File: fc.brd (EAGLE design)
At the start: 160 x 100 mm, 48 parts, among them IC1 FT230XQ, IC2 BN055, U2 ATMEGA2560-16AU100A-M, Y1 16MHz, Y2 32.768kHz

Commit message: First draft of the schematic finished
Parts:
- removed R20, R21: 5.6, rcl:R0603
- added LED0, LED5, LED6, LED7: (no value), led:CHIP-LED0603
- added PPM0, PPM1, PPM2, PPM3, PPM4, PPM5, PPM6, PPM7, SBUS: (no value), pinhead:1X03
- added R10, R11, R12: 100, rcl:R0603
- added R2: (no value), resistor:R0603
- added U$1: BSS138, hwp_SS18:SOT23
- R15, R16, R17: value 10k -> 100
- R18, R19: value 5.6 -> 100
- moved C18 154.7 mm to (17.8, 26.7), turned to 180 degrees
- moved C5 154.7 mm to (17.8, 30.5), turned to 180 degrees
- moved C4 153.9 mm to (3.81, 36.8), turned to 180 degrees
- moved C3 146.3 mm to (3.81, 33.0), turned to 180 degrees
- moved Y2 145.5 mm to (14.0, 27.9), turned to 270 degrees
- moved C2 138.7 mm to (3.81, 29.2), turned to 180 degrees
- moved R1 133.0 mm to (8.89, 33.0), turned to 180 degrees
- moved C1 129.8 mm to (3.81, 25.4), turned to 180 degrees
- moved C15 123.8 mm to (61.0, 35.6)
- moved LED_RX 123.8 mm to (77.5, 44.5)
- moved LED_TX 123.8 mm to (55.9, 31.8)
- moved R4 123.8 mm to (66.0, 22.9)
- moved C16 123.8 mm to (69.8, 35.6)
- moved C17 123.8 mm to (57.1, 27.9)
- moved IC2 120.2 mm to (8.89, 27.9), turned to 270 degrees
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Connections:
- removed net !ALERT_+3V3: R17.1, U2.8
- removed net !ALERT_+5V: R16.1, U2.7
- removed net !ALERT_VBAT: R15.1, U2.6
- removed net N$14: R21.2, U2.38
- removed net N$17: R20.2, U2.37
- removed net N$19: R18.2, U2.35
- removed net N$21: LED2.A, R19.1
- removed net N$23: LED4.A, R21.1
- new net !SBUS: R2.1, U$1.3, U2.12
- new net LED0: R15.2, U2.35
- new net LED1: R10.2, U2.36
- new net LED2: R11.2, U2.37
- new net LED3: R12.2, U2.38
- new net LED4: R16.2, U2.39
- new net LED5: R17.2, U2.40
- new net LED6: R18.2, U2.41
- new net LED7: R19.2, U2.42
- new net N$15: LED1.A, R10.1
- new net N$24: LED5.A, R17.1
- new net N$27: LED6.A, R18.1
- new net N$29: LED7.A, R19.1
- new net N$31: LED0.A, R15.1
- new net PPM0: PPM0.1, U2.24
- new net PPM1: PPM1.1, U2.25
- new net PPM2: PPM2.1, U2.26
- new net PPM3: PPM3.1, U2.5
- new net PPM4: PPM4.1, U2.6
- new net PPM5: PPM5.1, U2.7
- new net PPM6: PPM6.1, U2.15
- new net PPM7: PPM7.1, U2.16
- new net SBUS: SBUS.1, U$1.1
- net +3V3: now also R2.2; no longer R15.2, R16.2, R17.2
- net +5V: now also PPM0.2, PPM1.2, PPM2.2, PPM3.2, PPM4.2, PPM5.2, PPM6.2, PPM7.2, SBUS.2
- net GND: now also LED0.C, LED5.C, LED6.C, LED7.C, PPM0.3, PPM1.3, PPM2.3, PPM3.3, PPM4.3, PPM5.3, PPM6.3, PPM7.3, SBUS.3, U$1.2
- net N$18: now also LED2.A, R11.1; no longer R19.2, U2.36
- net N$20: now also LED3.A, R12.1; no longer LED1.A, R18.1
- net N$22: now also LED4.A, R16.1; no longer LED3.A, R20.1
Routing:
- net +3V3: track 0.00 -> 17.1 mm
- net N$25: track 0.00 -> 7.74 mm
- net N$13: track 0.00 -> 7.03 mm
- net N$12: track 0.00 -> 4.78 mm
- net N$1: track 0.00 -> 3.29 mm

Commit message: Initial draft for the layout
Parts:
- removed R13, R14: 10k, rcl:R0603
- moved C12 89.0 mm to (40.9, 37.4), turned to 180 degrees
- moved C11 88.7 mm to (41.0, 33.6), turned to 180 degrees
- moved R3 85.4 mm to (16.8, 27.7)
- moved C6 79.9 mm to (31.1, 32.4), flipped to the top, turned to 180 degrees
- moved C8 76.6 mm to (41.0, 30.0), turned to 180 degrees
- moved C7 75.8 mm to (31.0, 28.7), flipped to the top, turned to 180 degrees
- moved C9 70.5 mm to (41.1, 26.8), turned to 180 degrees
- moved C10 65.4 mm to (41.0, 23.7), turned to 180 degrees
- moved Y1 54.7 mm to (25.0, 30.5), flipped to the top, turned to 270 degrees
- moved U2 45.0 mm to (27.9, 31.8), turned to 90 degrees
- moved LED_RX 42.5 mm to (39.5, 25.4), turned to 270 degrees
- moved R5 27.4 mm to (43.2, 25.4), turned to 180 degrees
- moved LED7 26.8 mm to (2.39, 3.81)
- moved R19 26.8 mm to (2.39, 7.62)
- moved LED0 26.7 mm to (29.2, 3.81)
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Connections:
- removed net SCL: R13.1, U2.43
- removed net SDA: R14.1, U2.44
- net +3V3: now also C10.1, C11.1, C12.1, C15.1, C16.1, C17.1, C8.1, C9.1, IC1.1, IC1.10, IC1.8, ISP.2, LED_RX.A, LED_TX.A, R3.2, U2.10, U2.100, U2.31, U2.61, U2.80, U2.98; no longer R13.2, R14.2
- net +5V: no longer C10.1, C11.1, C12.1, C15.1, C16.1, C17.1, C8.1, C9.1, IC1.1, IC1.10, IC1.8, ISP.2, LED_RX.A, LED_TX.A, R3.2, U2.10, U2.100, U2.31, U2.61, U2.80, U2.98
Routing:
- net +3V3: track 17.1 -> 191.2 mm, vias 0 -> 7
- net +5V: track 0.00 -> 71.1 mm
- net LED0: track 0.00 -> 57.3 mm, vias 0 -> 1
- net LED1: track 0.00 -> 54.4 mm, vias 0 -> 1
- net LED2: track 0.00 -> 51.3 mm, vias 0 -> 1
- net LED3: track 0.00 -> 48.1 mm, vias 0 -> 1
- net LED4: track 0.00 -> 45.6 mm, vias 0 -> 1
- net LED5: track 0.00 -> 42.5 mm, vias 0 -> 1
- net LED6: track 0.00 -> 39.4 mm, vias 0 -> 1
- net !RESET: track 0.00 -> 38.6 mm, vias 0 -> 2
- net LED7: track 0.00 -> 36.6 mm, vias 0 -> 1
- net MISO: track 0.00 -> 33.0 mm
- net SCK: track 0.00 -> 30.1 mm
- net MOSI: track 0.00 -> 28.5 mm
- net PPM0: track 0.00 -> 22.5 mm
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- added copper zone on layer 1, net GND
- added copper zone on layer 16, net GND

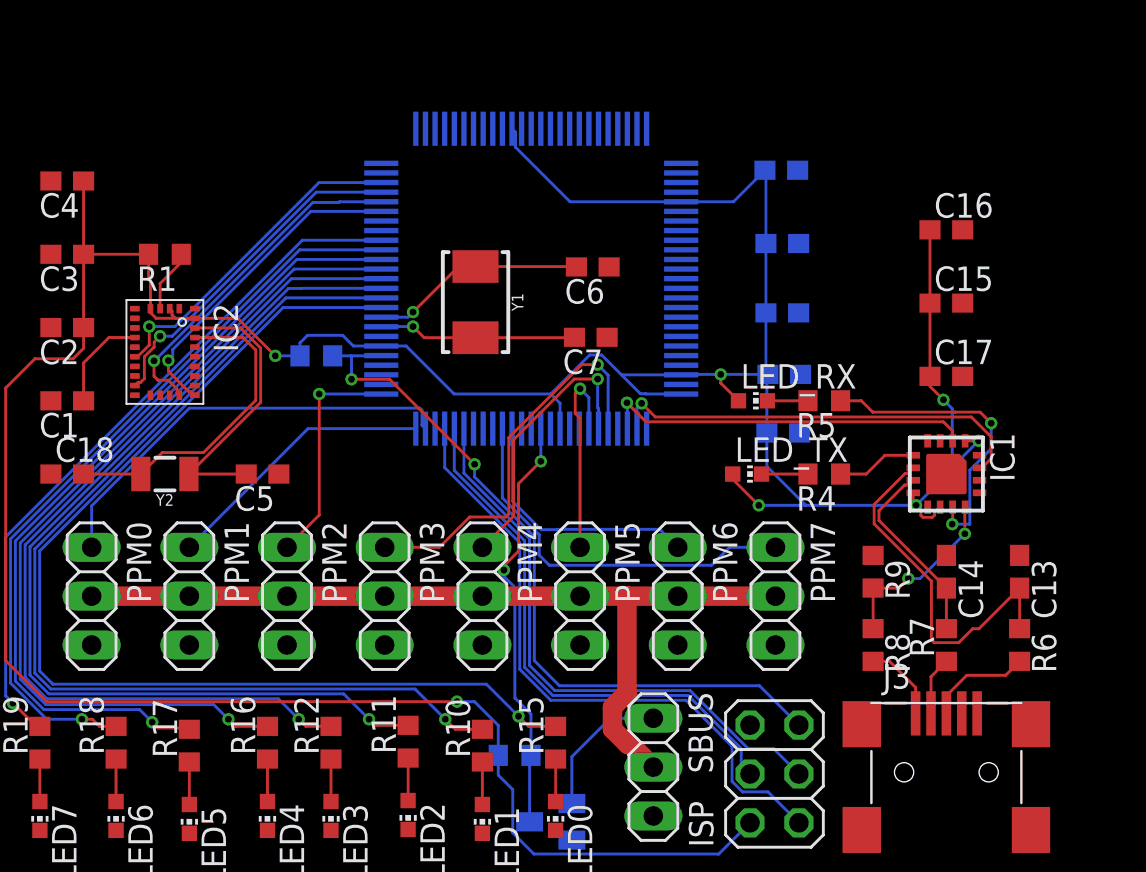
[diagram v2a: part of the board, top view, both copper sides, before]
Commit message: Small changes, added reset button
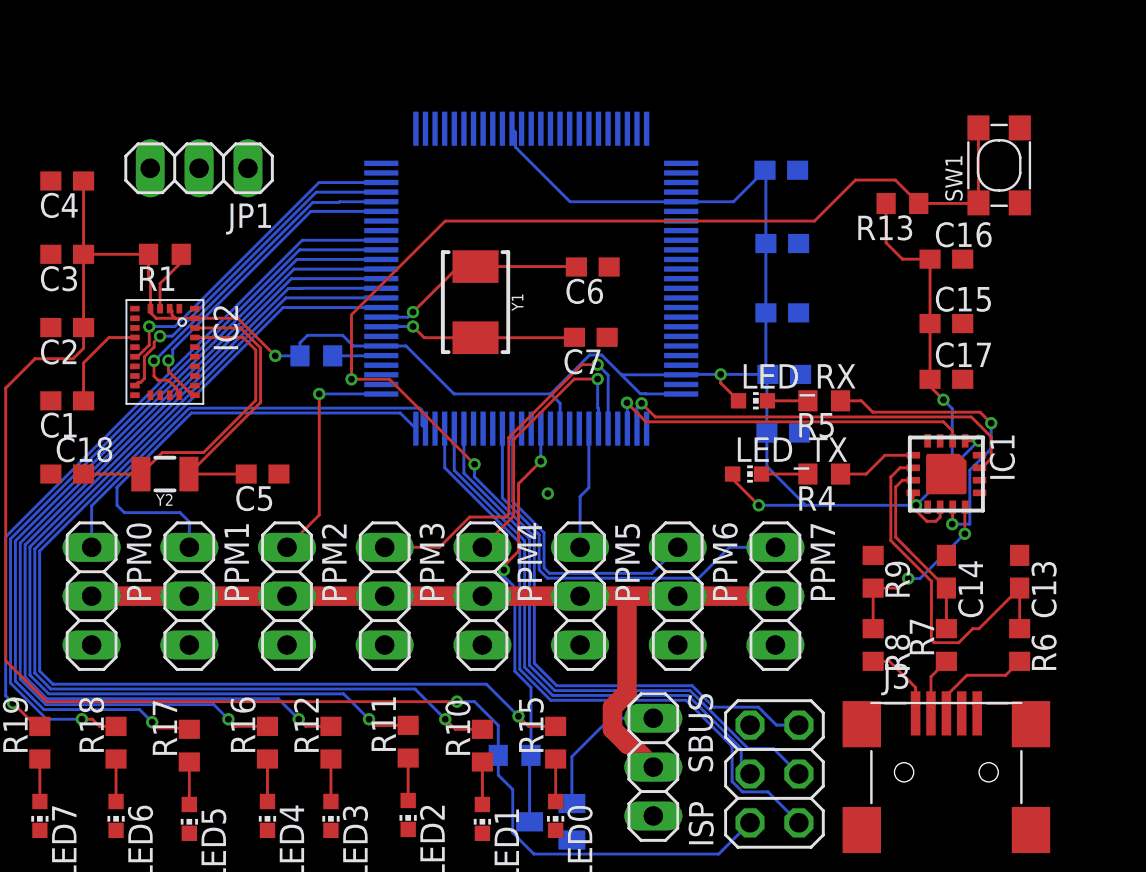
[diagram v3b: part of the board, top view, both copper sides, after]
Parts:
- added JP1: (no value), pinhead:1X03
- added R13: 10k, resistor:R0603
- added SW1: DHT-4235A, Seeed-Switch:SW4-SMD-4.2X3.2X2.5MM
- moved C16 1.52 mm to (49.5, 32.8)
- moved C15 1.07 mm to (49.5, 29.4)
- moved C17 0.15 mm to (49.5, 26.5)
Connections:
- net !RESET: now also R13.1, SW1.1, SW1.2
- net +3V3: now also R13.2
- net +5V: now also JP1.2
- net GND: now also JP1.1, JP1.3, SW1.3, SW1.4
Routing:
- net !RESET: track 38.6 -> 82.0 mm
- net PPM1: track 14.3 -> 23.9 mm
- net PPM5: track 10.7 -> 6.36 mm, vias 1 -> 0
- net +3V3: track 191.2 -> 194.7 mm
- net PPM6: track 13.4 -> 15.6 mm
- net PPM7: track 20.3 -> 21.3 mm
- net N$5: track 10.4 -> 9.93 mm

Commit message: Improved the design
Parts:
- removed C13, C14: 47pF, rcl:C0603
- removed C6, C7: 8pF, rcl:C0603
- removed C8, C9: 100nF, rcl:C0603
- removed IC1: FT230XQ, ftdichip:QFN16
- removed ISP: (no value), pinhead:2X03
- removed J3: (no value), adafruit:USB-MINIB
- removed LED_RX, LED_TX: (no value), led:CHIP-LED0603
- removed R13: 10k, resistor:R0603
- removed R3: 10k, rcl:R0603
- removed R4, R5: 5.6, rcl:R0603
- removed R6, R7: 27, rcl:R0603
- removed R8: 4k7, rcl:R0603
- removed SW1: DHT-4235A, Seeed-Switch:SW4-SMD-4.2X3.2X2.5MM
- removed U2: ATMEGA2560-16AU100A-M, ATMEGA2560:100A-M
- removed Y1: 16MHz, SparkFun-Clocks:CRYSTAL-SMD-5X3.2-2PAD
- added C19, C20: 8pF, rcl:C0603
- added C21, C22, C23, C24, C25: 100nF, rcl:C0603
- added ISP1: (no value), pinhead:2X03
- added J2: USBC, USBC:USBC
- added LED_RX1, LED_TX1: (no value), led:CHIP-LED0603
- added R14: 270, rcl:R0603
- added R20, R21: 27, rcl:R0603
- added R22, R23: 4k7, rcl:R0603
- added R35: 10k, resistor:R0603
- added S2: FSMSM, switch:SWITCH_FSMSM
- added U1: ATMEGA2560-16AU100A-M, ATMEGA2560:100A-M
- added U4: FT230XQ, ftdichip:QFN16
- added U5: (no value), SI8621AB-B-IS:SO08
- added Y3: 16MHz, SparkFun-Clocks:CRYSTAL-SMD-5X3.2-2PAD
- C10, C11: value 100nF -> 47pF
- C12: value 100nF -> 10nF
- C17: device rcl:C0603 -> Kondensatoren (rev17a):2.6X1.6X1(BXCXA)
- R9: value 10k -> 270
- moved JP1 37.2 mm to (47.9, 36.5)
- moved C12 29.2 mm to (52.2, 10.4), flipped to the top, turned to 90 degrees
- moved R15 22.9 mm to (6.29, 7.00)
- moved LED0 22.9 mm to (6.29, 4.00)
- moved C17 22.7 mm to (37.6, 7.20), turned to 90 degrees
- moved C16 22.4 mm to (50.1, 10.4), turned to 90 degrees
- moved C11 21.3 mm to (46.4, 13.0), flipped to the top
- moved R19 19.0 mm to (21.3, 7.00)
- moved LED7 18.9 mm to (21.3, 3.80)
- moved R10 17.0 mm to (8.40, 7.00)
- moved LED1 17.0 mm to (8.40, 4.00)
- moved C10 13.7 mm to (49.5, 13.0), flipped to the top
- moved R18 12.8 mm to (19.1, 7.00)
- moved LED6 12.7 mm to (19.1, 4.00)
- moved R11 11.0 mm to (10.6, 7.00)
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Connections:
- removed net N$10: J3.D+, R6.2
- removed net N$11: J3.D-, R7.1
- removed net N$16: J3.VBUS, R8.2
- removed net N$6: IC1.5, R4.1
- removed net N$7: IC1.11, R5.1
- removed net N$8: LED_TX.C, R4.2
- removed net N$9: LED_RX.C, R5.2
- removed net VBUS_SENSE: IC1.12, R8.1, R9.2
- new net D+1: J2.A6, J2.B6, R20.2
- new net D-1: J2.A7, J2.B7, R21.1
- new net GNDIO: C10.1, C11.1, C12.2, C15.2, C16.2, C17.2, J2.A1, J2.A12, J2.S1, J2.S2, J2.S3, J2.S4, U4.13, U4.3, U5.4
- new net N$32: C19.2, U1.34, Y3.P$2
- new net N$33: C20.2, U1.33, Y3.P$1
- new net RXD: R23.1, U4.2, U5.3
- new net TXD: R22.1, U4.15, U5.2
- new net USBDM1: C11.2, R21.2, U4.7
- new net USBDP1: C10.2, R20.1, U4.6
- new net VBUS: C12.1, C16.1, C17.1, J2.A4, J2.A9, U4.10
- new net VCCIO: C15.1, LED_RX1.A, LED_TX1.A, R22.2, R23.2, U4.1, U4.16, U4.8, U5.1
- net !BNO_RST: now also U1.47; no longer U2.48
- net !RESET: now also ISP1.5, R35.1, S2.2, U1.30; no longer ISP.5, R13.1, R3.1, SW1.1, SW1.2, U2.30
- net !SBUS: now also U1.12; no longer U2.12
- net +3V3: now also C21.1, C22.1, C23.1, C24.1, C25.1, ISP1.2, R35.2, U1.10, U1.100, U1.31, U1.61, U1.80, U1.98, U5.8; no longer C10.1, C11.1, C12.1, C15.1, C16.1, C17.1, C8.1, C9.1, IC1.1, IC1.10, IC1.8, ISP.2, LED_RX.A, LED_TX.A, R13.2, R3.2, U2.10, U2.100, U2.31, U2.61, U2.80, U2.98
- net BNO_INT: now also U1.23; no longer U2.47
- net BNO_RX: now also U1.46; no longer U2.46
- net BNO_TX: now also U1.45; no longer U2.45
- net GND: now also C19.1, C20.1, C21.2, C22.2, C23.2, C24.2, C25.2, ISP1.6, S2.1, U1.11, U1.32, U1.62, U1.81, U1.99, U5.5; no longer C10.2, C11.2, C12.2, C13.1, C14.1, C15.2, C16.2, C17.2, C6.1, C7.1, C8.2, C9.2, IC1.13, IC1.3, ISP.6, J3.GND, R9.1, SW1.3, SW1.4, U2.11, U2.32, U2.62, U2.81, U2.99
- net LED0: now also U1.35; no longer U2.35
- net LED1: now also U1.36; no longer U2.36
- net LED2: now also U1.37; no longer U2.37
- net LED3: now also U1.38; no longer U2.38
- net LED4: now also U1.39; no longer U2.39
- net LED5: now also U1.40; no longer U2.40
- net LED6: now also U1.41; no longer U2.41
- net LED7: now also U1.42; no longer U2.42
- net MISO: now also ISP1.1, U1.22; no longer ISP.1, U2.22
- net MOSI: now also ISP1.4, U1.21; no longer ISP.4, U2.21
- net N$2: now also R14.1, U4.11; no longer C6.2, U2.34, Y1.P$2
- net N$3: now also LED_RX1.C, R9.2; no longer C7.2, U2.33, Y1.P$1
- net N$4: now also LED_TX1.C, R14.2; no longer C13.2, IC1.6, R6.1
- net N$5: now also R9.1, U4.5; no longer C14.2, IC1.7, R7.2
- net PPM0: now also U1.24; no longer U2.24
- net PPM1: now also U1.25; no longer U2.25
- net PPM2: now also U1.26; no longer U2.26
- net PPM3: now also U1.5; no longer U2.5
- net PPM4: now also U1.6; no longer U2.6
- net PPM5: now also U1.7; no longer U2.7
- net PPM6: now also U1.15; no longer U2.15
- net PPM7: now also U1.16; no longer U2.16
- net SCK: now also ISP1.3, U1.20; no longer ISP.3, U2.20
- net USB_RX: now also U1.2, U5.7; no longer IC1.15, U2.2
- net USB_TX: now also U1.3, U5.6; no longer IC1.2, U2.3
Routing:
- net GNDIO: track 0.00 -> 74.6 mm, vias 0 -> 2
- net +3V3: track 194.7 -> 125.3 mm, vias 7 -> 2
- net !RESET: track 82.0 -> 39.7 mm, vias 2 -> 3
- net VCCIO: track 0.00 -> 28.7 mm, vias 0 -> 2
- net VBUS: track 0.00 -> 27.7 mm, vias 0 -> 2
- net +5V: track 71.1 -> 95.8 mm
- net PPM5: track 6.36 -> 29.7 mm, vias 0 -> 1
- net LED0: track 57.3 -> 37.2 mm, vias 1 -> 2
- net !SBUS: track 21.8 -> 40.1 mm, vias 2 -> 4
- net PPM2: track 11.9 -> 29.2 mm
- net N$4: track 18.6 -> 1.91 mm
- net PPM6: track 15.6 -> 31.6 mm, vias 0 -> 1
- net LED1: track 54.4 -> 38.5 mm, vias 1 -> 2
- net N$7: track 15.8 -> 0.00 mm, vias 2 -> 0
- net MISO: track 33.0 -> 17.5 mm, vias 0 -> 1
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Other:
- board size 160 x 100 mm -> 55 x 40 mm

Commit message: Spannungsregler
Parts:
- added C13, C9: 22uF, SparkFun-Capacitors:0805
- added C14: 1nF, SparkFun-Capacitors:0603
- added R5: 35.7k, SparkFun-Resistors:0603
- added R6: 11.5k, SparkFun-Resistors:0603
- added U3: LMZ21700, jonas_ti:SIL0008E
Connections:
- new net N$8: R5.1, R6.2, U3.P2
- new net N$9: C14.1, U3.P1
- net +3V3: now also C9.1, R5.2, U3.P4, U3.P6
- net +5V: now also C13.1, U3.P7, U3.P8
- net GND: now also C13.2, C14.2, C9.2, R6.1, U3.P10, U3.P5, U3.P9
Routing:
- net +3V3: track 125.3 -> 138.4 mm
- net +5V: track 95.8 -> 108.3 mm
- net N$8: track 0.00 -> 3.05 mm
- net N$9: track 0.00 -> 1.92 mm
- net USB_TX: track 26.8 -> 28.2 mm
- net !RESET: track 39.7 -> 38.8 mm
- net PPM4: track 26.8 -> 26.3 mm

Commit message: FTDI hauptsächlich
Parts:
- removed C24, C25: 100nF, rcl:C0603
- removed LED0: (no value), led:CHIP-LED0603
- removed PPM0: (no value), pinhead:1X03
- removed R20, R21: 27, rcl:R0603
- removed R22, R23: 4k7, rcl:R0603
- removed U5: (no value), SI8621AB-B-IS:SO08
- added C7, C8: 100n, resistor:C0603
- added LED8: (no value), led:CHIP-LED0603
- added PPM8: (no value), pinhead:1X03
- added R13: 100, rcl:R0603
- added R4: 10k, resistor:R0603
- added R7: 4.7k, SparkFun-Resistors:0603
- added R8: 270, SparkFun-Resistors:0603
- added U2: ATMEGA2560-16AU100A-M, ATMEGA2560:100A-M
- C1: value 100n -> 22uF; device resistor:C0603 -> SparkFun-Capacitors:0805
- C10: value 47pF -> 8pF
- C11: value 47pF -> 120n; device rcl:C0603 -> resistor:C0603
- C12: value 10nF -> 100nF
- C13: value 22uF -> 6.8n; device SparkFun-Capacitors:0805 -> resistor:C0603
- C14: value 1nF -> 0.1uF
- C16: value 100nF -> 22p; device rcl:C0603 -> resistor:C0603
- C17: value 4.7µF -> 22p; device Kondensatoren (rev17a):2.6X1.6X1(BXCXA) -> resistor:C0603
- C18: value 22p -> 47pF; device resistor:C0603 -> SparkFun-Capacitors:0603
- C19: value 8pF -> 47pF; device rcl:C0603 -> SparkFun-Capacitors:0603
- C2: value 6.8n -> 22uF; device resistor:C0603 -> SparkFun-Capacitors:0805
- C20: value 8pF -> 0.1uF; device rcl:C0603 -> SparkFun-Capacitors:0603
- C21: value 100nF -> 10nF; device rcl:C0603 -> SparkFun-Capacitors:0603
- C22: value 100nF -> 4.7uF; device rcl:C0603 -> SparkFun-Capacitors:0603
- C3: value 120n -> 1nF; device resistor:C0603 -> SparkFun-Capacitors:0603
- C4: value 100n -> 8pF; device resistor:C0603 -> rcl:C0603
- C5: value 22p -> 100nF; device resistor:C0603 -> rcl:C0603
- C9: value 22uF -> 100nF; device SparkFun-Capacitors:0805 -> rcl:C0603
- LED_RX1, LED_TX1: device led:CHIP-LED0603 -> SparkFun-LED:LED-0603
- R1: value 10k -> 35.7k; device resistor:R0603 -> SparkFun-Resistors:0603
- R10: value 100 -> 27; device rcl:R0603 -> SparkFun-Resistors:0603
- R14: value 270 -> 100
- R19: value 100 -> (none); device rcl:R0603 -> resistor:R0603
- R2: value (none) -> 11.5k; device resistor:R0603 -> SparkFun-Resistors:0603
- R5: value 35.7k -> 270
- R6: value 11.5k -> 4.7k
- R9: value 270 -> 27; device rcl:R0603 -> SparkFun-Resistors:0603
- U1: value ATMEGA2560-16AU100A-M -> LMZ21700; device ATMEGA2560:100A-M -> jonas_ti:SIL0008E
- U3: value LMZ21700 -> (none); device jonas_ti:SIL0008E -> SI8621AB-B-IS:SO08
- moved C16 47.4 mm to (3.81, 20.6), turned to 0 degrees
- moved C11 44.2 mm to (3.81, 24.8)
- moved C18 43.5 mm to (46.6, 12.9)
- moved R14 42.3 mm to (12.7, 7.00), turned to 90 degrees
- moved C20 42.0 mm to (50.6, 10.4), turned to 90 degrees
- moved C2 41.5 mm to (42.8, 36.8), turned to 90 degrees
- moved R10 40.7 mm to (49.0, 10.4), turned to 270 degrees
- moved C19 36.9 mm to (49.8, 12.9)
- moved C10 36.6 mm to (14.9, 24.9)
- moved C13 36.4 mm to (3.81, 22.6), turned to 180 degrees
- moved C3 34.7 mm to (37.4, 33.4), turned to 270 degrees
- moved R2 31.7 mm to (39.9, 32.8)
- moved C1 31.5 mm to (37.2, 37.0), turned to 270 degrees
- moved C5 30.4 mm to (40.0, 31.0), turned to 0 degrees
- moved R1 30.0 mm to (39.9, 34.3), turned to 0 degrees
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- renumbered C23 to C6, IC2 to IC1, J2 to J1, R35 to R3, S2 to S1, Y3 to Y1
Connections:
- net !BNO_RST: now also U2.47; no longer U1.47
- net !RESET: now also U2.30; no longer U1.30
- net !SBUS: now also R19.1, U2.12; no longer R2.1, U1.12
- net +3V3: now also C11.1, C12.1, C13.1, C15.1, C5.1, C8.1, R19.2, R4.2, U1.P4, U1.P6, U2.10, U2.100, U2.31, U2.61, U2.80, U2.98, U3.8; no longer C21.1, C22.1, C24.1, C25.1, C3.1, C4.1, R2.2, R5.2, U1.10, U1.100, U1.31, U1.61, U1.80, U1.98, U3.P4, U3.P6, U5.8
- net +5V: now also C1.1, PPM8.2, U1.P7, U1.P8; no longer C13.1, PPM0.2, U3.P7, U3.P8
- net BNO_INT: now also U2.23; no longer U1.23
- net BNO_RX: now also U2.46; no longer U1.46
- net BNO_TX: now also U2.45; no longer U1.45
- net D+1: now also R10.2; no longer R20.2
- net D-1: now also R9.1; no longer R21.1
- net GND: now also C10.1, C11.2, C12.2, C15.2, C16.1, C17.1, C4.1, C5.2, C7.2, C8.2, LED8.C, PPM8.3, R2.1, U1.P10, U1.P5, U1.P9, U2.11, U2.32, U2.62, U2.81, U2.99, U3.5; no longer C14.2, C18.1, C19.1, C20.1, C21.2, C22.2, C24.2, C25.2, C4.2, C5.1, LED0.C, PPM0.3, R6.1, U1.11, U1.32, U1.62, U1.81, U1.99, U3.P10, U3.P5, U3.P9, U5.5
- net GNDIO: now also C14.2, C18.1, C19.1, C20.2, C21.2, C22.2, U3.4; no longer C10.1, C11.1, C12.2, C15.2, C16.2, C17.2, U5.4
- net LED0: now also R11.2, U2.35; no longer R15.2, U1.35
- net LED1: now also R12.2, U2.36; no longer R10.2, U1.36
- net LED2: now also R13.2, U2.37; no longer R11.2, U1.37
- net LED3: now also R14.2, U2.38; no longer R12.2, U1.38
- net LED4: now also R15.2, U2.39; no longer R16.2, U1.39
- net LED5: now also R16.2, U2.40; no longer R17.2, U1.40
- net LED6: now also R17.2, U2.41; no longer R18.2, U1.41
- net LED7: now also R18.2, U2.42; no longer R19.2, U1.42
- net MISO: now also U2.22; no longer U1.22
- net MOSI: now also U2.21; no longer U1.21
- net N$1: now also R4.1; no longer R1.1
- net N$12: now also C7.1; no longer C1.1
- net N$13: now also C17.2; no longer C5.2
- net N$15: now also LED2.A, R12.1; no longer LED1.A, R10.1
- net N$18: now also LED3.A, R13.1; no longer LED2.A, R11.1
- net N$2: now also R5.1; no longer R14.1
- net N$20: now also LED4.A, R14.1; no longer LED3.A, R12.1
- net N$22: now also LED5.A, R15.1; no longer LED4.A, R16.1
- net N$24: now also LED6.A, R16.1; no longer LED5.A, R17.1
- net N$25: now also C16.2; no longer C18.2
- net N$27: now also LED7.A, R17.1; no longer LED6.A, R18.1
- net N$29: now also LED8.A, R18.1; no longer LED7.A, R19.1
- net N$3: now also R8.2; no longer R9.2
- net N$31: now also LED1.A, R11.1; no longer LED0.A, R15.1
- net N$32: now also C10.2, U2.34; no longer C19.2, U1.34
- net N$33: now also C4.2, U2.33; no longer C20.2, U1.33
- net N$4: now also R5.2; no longer R14.2
- net N$5: now also R8.1; no longer R9.1
- net N$8: now also R1.1, R2.2, U1.P2; no longer R5.1, R6.2, U3.P2
- net N$9: now also C3.1, U1.P1; no longer C14.1, U3.P1
- net PPM0: now also PPM1.1, U2.24; no longer PPM0.1, U1.24
- net PPM1: now also PPM2.1, U2.25; no longer PPM1.1, U1.25
- net PPM2: now also PPM3.1, U2.26; no longer PPM2.1, U1.26
- net PPM3: now also PPM4.1, U2.5; no longer PPM3.1, U1.5
- net PPM4: now also PPM5.1, U2.6; no longer PPM4.1, U1.6
- net PPM5: now also PPM6.1, U2.7; no longer PPM5.1, U1.7
- net PPM6: now also PPM7.1, U2.15; no longer PPM6.1, U1.15
- net PPM7: now also PPM8.1, U2.16; no longer PPM7.1, U1.16
- net RXD: now also R7.1, U3.3; no longer R23.1, U5.3
- net SCK: now also U2.20; no longer U1.20
- net TXD: now also R6.1, U3.2; no longer R22.1, U5.2
- net USBDM1: now also C18.2, R9.2; no longer C11.2, R21.2
- net USBDP1: now also C19.2, R10.1; no longer C10.2, R20.1
- net USB_RX: now also U2.2, U3.7; no longer U1.2, U5.7
- net USB_TX: now also U2.3, U3.6; no longer U1.3, U5.6
- net VBUS: now also C20.1, C21.1, C22.1; no longer C12.1, C16.1, C17.1
- net VCCIO: now also C14.1, R6.2, R7.2, U3.1; no longer C15.1, R22.2, R23.2, U5.1
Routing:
- net GNDIO: track 74.6 -> 28.9 mm, vias 2 -> 6
- net VBUS: track 27.7 -> 21.2 mm
- net USBDM1: track 10.4 -> 7.15 mm
- net TXD: track 12.1 -> 10.9 mm
- net N$3: track 5.61 -> 6.62 mm, vias 2 -> 0
- net +5V: track 108.3 -> 109.3 mm
- net N$5: track 3.59 -> 2.73 mm
- net LED7: track 47.3 -> 46.5 mm
- net USBDP1: track 5.65 -> 4.96 mm
- net RXD: track 11.4 -> 12.1 mm
- net VCCIO: track 28.7 -> 28.1 mm, vias 2 -> 3
- added copper zone on layer 1, net GNDIO
- added copper zone on layer 16, net GNDIO
